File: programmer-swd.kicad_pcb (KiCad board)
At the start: 2 copper layers, 26.8 x 12.2 mm, 3 parts, among them J1 MOLEX, J2 Conn_01x04_Pin, J3 Conn_01x04_Pin

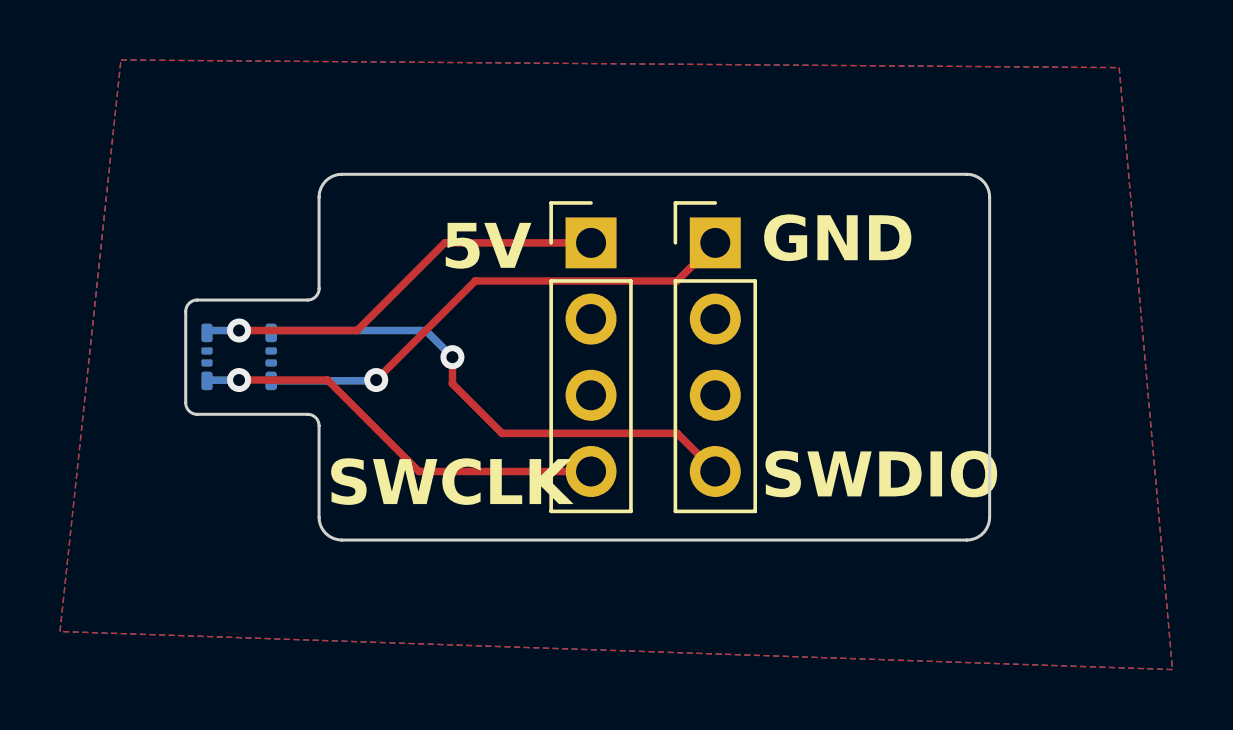
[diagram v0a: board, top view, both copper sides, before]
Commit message: Fixed header connections
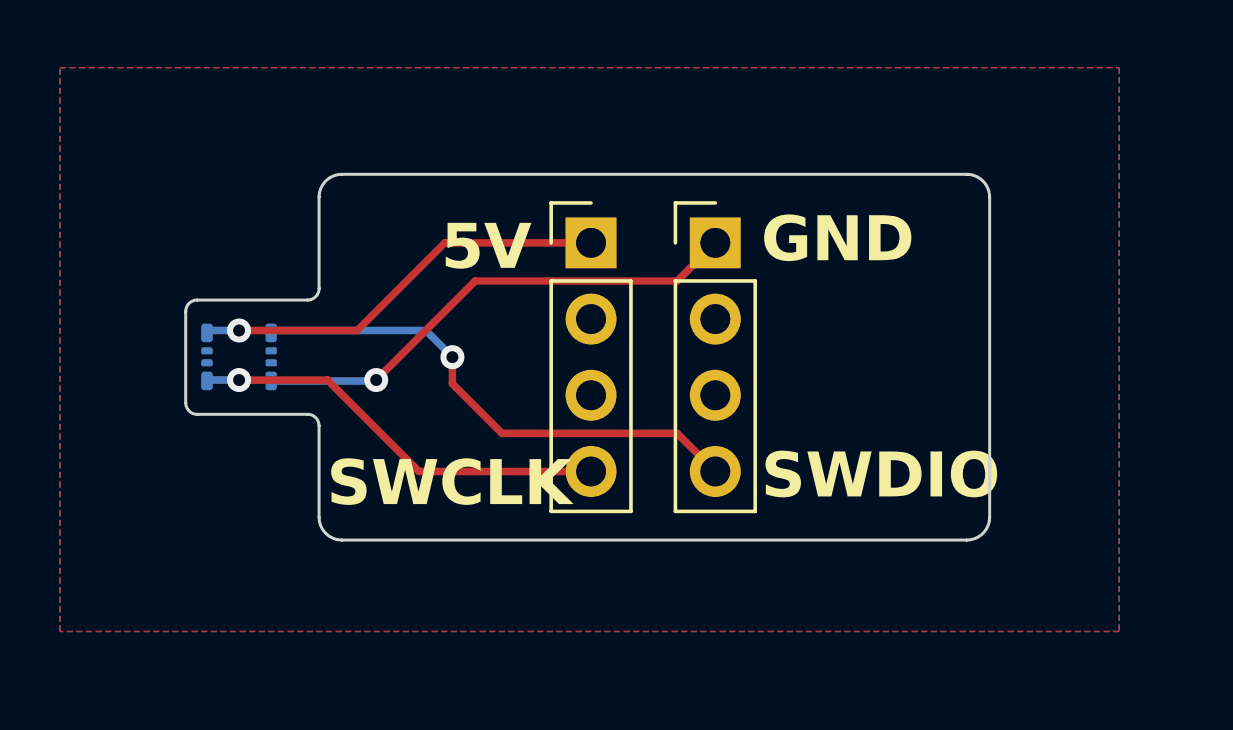
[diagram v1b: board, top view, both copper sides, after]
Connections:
- J1 pad 2: Net-(J2-Pin_3) -> unconnected-(J1-Pad2)
- J1 pad 3: Net-(J2-Pin_2) -> unconnected-(J1-Pad3)
- J1 pad 6: Net-(J3-Pin_3) -> unconnected-(J1-Pad6)
- J1 pad 7: Net-(J3-Pin_2) -> unconnected-(J1-Pad7)
- J2 pad 2: Net-(J2-Pin_2) -> unconnected-(J2-Pin_2-Pad2)
- J2 pad 3: Net-(J2-Pin_3) -> unconnected-(J2-Pin_3-Pad3)
- J3 pad 2: Net-(J3-Pin_2) -> unconnected-(J3-Pin_2-Pad2)
- J3 pad 3: Net-(J3-Pin_3) -> unconnected-(J3-Pin_3-Pad3)
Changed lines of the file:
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@@
   (net 0 "")
   (net 1 "GND")
-  (net 2 "Net-(J2-Pin_3)")
-  (net 3 "Net-(J2-Pin_2)")
+  (net 2 "unconnected-(J1-Pad2)")
+  (net 3 "unconnected-(J1-Pad3)")
   (net 4 "/IO")
   (net 5 "+5V")
-  (net 6 "Net-(J3-Pin_3)")
-  (net 7 "Net-(J3-Pin_2)")
+  (net 6 "unconnected-(J1-Pad6)")
+  (net 7 "unconnected-(J1-Pad7)")
   (net 8 "/CLK")
+  (net 9 "unconnected-(J2-Pin_2-Pad2)")
+  (net 10 "unconnected-(J2-Pin_3-Pad3)")
+  (net 11 "unconnected-(J3-Pin_2-Pad2)")
+  (net 12 "unconnected-(J3-Pin_3-Pad3)")
   (footprint "Connector_PinHeader_2.54mm:PinHeader_1x04_P2.54mm_Vertical" (layer "F.Cu")
     (at 155.702 98.044)
@@
       (net 1 "GND") (pinfunction "Pin_1") (pintype "passive"))
     (pad "2" thru_hole oval (at 0 2.54) (size 1.7 1.7) (drill 1) (layers "*.Cu" "*.Mask")
-      (net 7 "Net-(J3-Pin_2)") (pinfunction "Pin_2") (pintype "passive"))
+      (net 11 "unconnected-(J3-Pin_2-Pad2)") (pinfunction "Pin_2") (pintype "passive+no_connect"))
     (pad "3" thru_hole oval (at 0 5.08) (size 1.7 1.7) (drill 1) (layers "*.Cu" "*.Mask")
-      (net 6 "Net-(J3-Pin_3)") (pinfunction "Pin_3") (pintype "passive"))
+      (net 12 "unconnected-(J3-Pin_3-Pad3)") (pinfunction "Pin_3") (pintype "passive+no_connect"))
     (pad "4" thru_hole oval (at 0 7.62) (size 1.7 1.7) (drill 1) (layers "*.Cu" "*.Mask")
       (net 4 "/IO") (pinfunction "Pin_4") (pintype "passive"))
@@
       (net 5 "+5V") (pinfunction "Pin_1") (pintype "passive"))
     (pad "2" thru_hole oval (at 0 2.54) (size 1.7 1.7) (drill 1) (layers "*.Cu" "*.Mask")
-      (net 3 "Net-(J2-Pin_2)") (pinfunction "Pin_2") (pintype "passive"))
+      (net 9 "unconnected-(J2-Pin_2-Pad2)") (pinfunction "Pin_2") (pintype "passive+no_connect"))
     (pad "3" thru_hole oval (at 0 5.08) (size 1.7 1.7) (drill 1) (layers "*.Cu" "*.Mask")
-      (net 2 "Net-(J2-Pin_3)") (pinfunction "Pin_3") (pintype "passive"))
+      (net 10 "unconnected-(J2-Pin_3-Pad3)") (pinfunction "Pin_3") (pintype "passive+no_connect"))
     (pad "4" thru_hole oval (at 0 7.62) (size 1.7 1.7) (drill 1) (layers "*.Cu" "*.Mask")
       (net 8 "/CLK") (pinfunction "Pin_4") (pintype "passive"))
@@
       (net 8 "/CLK") (pintype "input") (thermal_bridge_angle 45))
     (pad "2" smd roundrect (at -0.2 -1.07 90) (size 0.24 0.38) (layers "B.Cu" "B.Paste" "B.Mask") (roundrect_rratio 0.25)
-      (net 2 "Net-(J2-Pin_3)") (pintype "input") (thermal_bridge_angle 45))
+      (net 2 "unconnected-(J1-Pad2)") (pintype "input+no_connect") (thermal_bridge_angle 45))
     (pad "3" smd roundrect (at 0.2 -1.07 90) (size 0.24 0.38) (layers "B.Cu" "B.Paste" "B.Mask") (roundrect_rratio 0.25)
-      (net 3 "Net-(J2-Pin_2)") (pintype "input") (thermal_bridge_angle 45))
+      (net 3 "unconnected-(J1-Pad3)") (pintype "input+no_connect") (thermal_bridge_angle 45))
     (pad "4" smd roundrect (at 0.8 -1.07 90) (size 0.62 0.38) (layers "B.Cu" "B.Paste" "B.Mask") (roundrect_rratio 0.25)
       (net 5 "+5V") (pintype "input") (thermal_bridge_angle 45))
@@
       (net 4 "/IO") (pintype "input") (thermal_bridge_angle 45))
     (pad "6" smd roundrect (at 0.2 1.07 90) (size 0.24 0.38) (layers "B.Cu" "B.Paste" "B.Mask") (roundrect_rratio 0.25)
-      (net 6 "Net-(J3-Pin_3)") (pintype "input") (thermal_bridge_angle 45))
+      (net 6 "unconnected-(J1-Pad6)") (pintype "input+no_connect") (thermal_bridge_angle 45))
     (pad "7" smd roundrect (at -0.2 1.07 90) (size 0.24 0.38) (layers "B.Cu" "B.Paste" "B.Mask") (roundrect_rratio 0.25)
-      (net 7 "Net-(J3-Pin_2)") (pintype "input") (thermal_bridge_angle 45))
+      (net 7 "unconnected-(J1-Pad7)") (pintype "input+no_connect") (thermal_bridge_angle 45))
     (pad "8" smd roundrect (at -0.8 1.07 90) (size 0.62 0.38) (layers "B.Cu" "B.Paste" "B.Mask") (roundrect_rratio 0.25)
       (net 1 "GND") (pintype "input") (thermal_bridge_angle 45))
@@
     (polygon
       (pts
-        (xy 135.89 91.948)
+        (xy 133.858 92.202)
         (xy 169.164 92.202)
-        (xy 170.942 112.268)
+        (xy 169.164 110.998)
         (xy 133.858 110.998)
       )
